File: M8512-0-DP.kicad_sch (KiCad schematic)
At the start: 1 part, among them J1 KL10_6-bay_backplane_connector

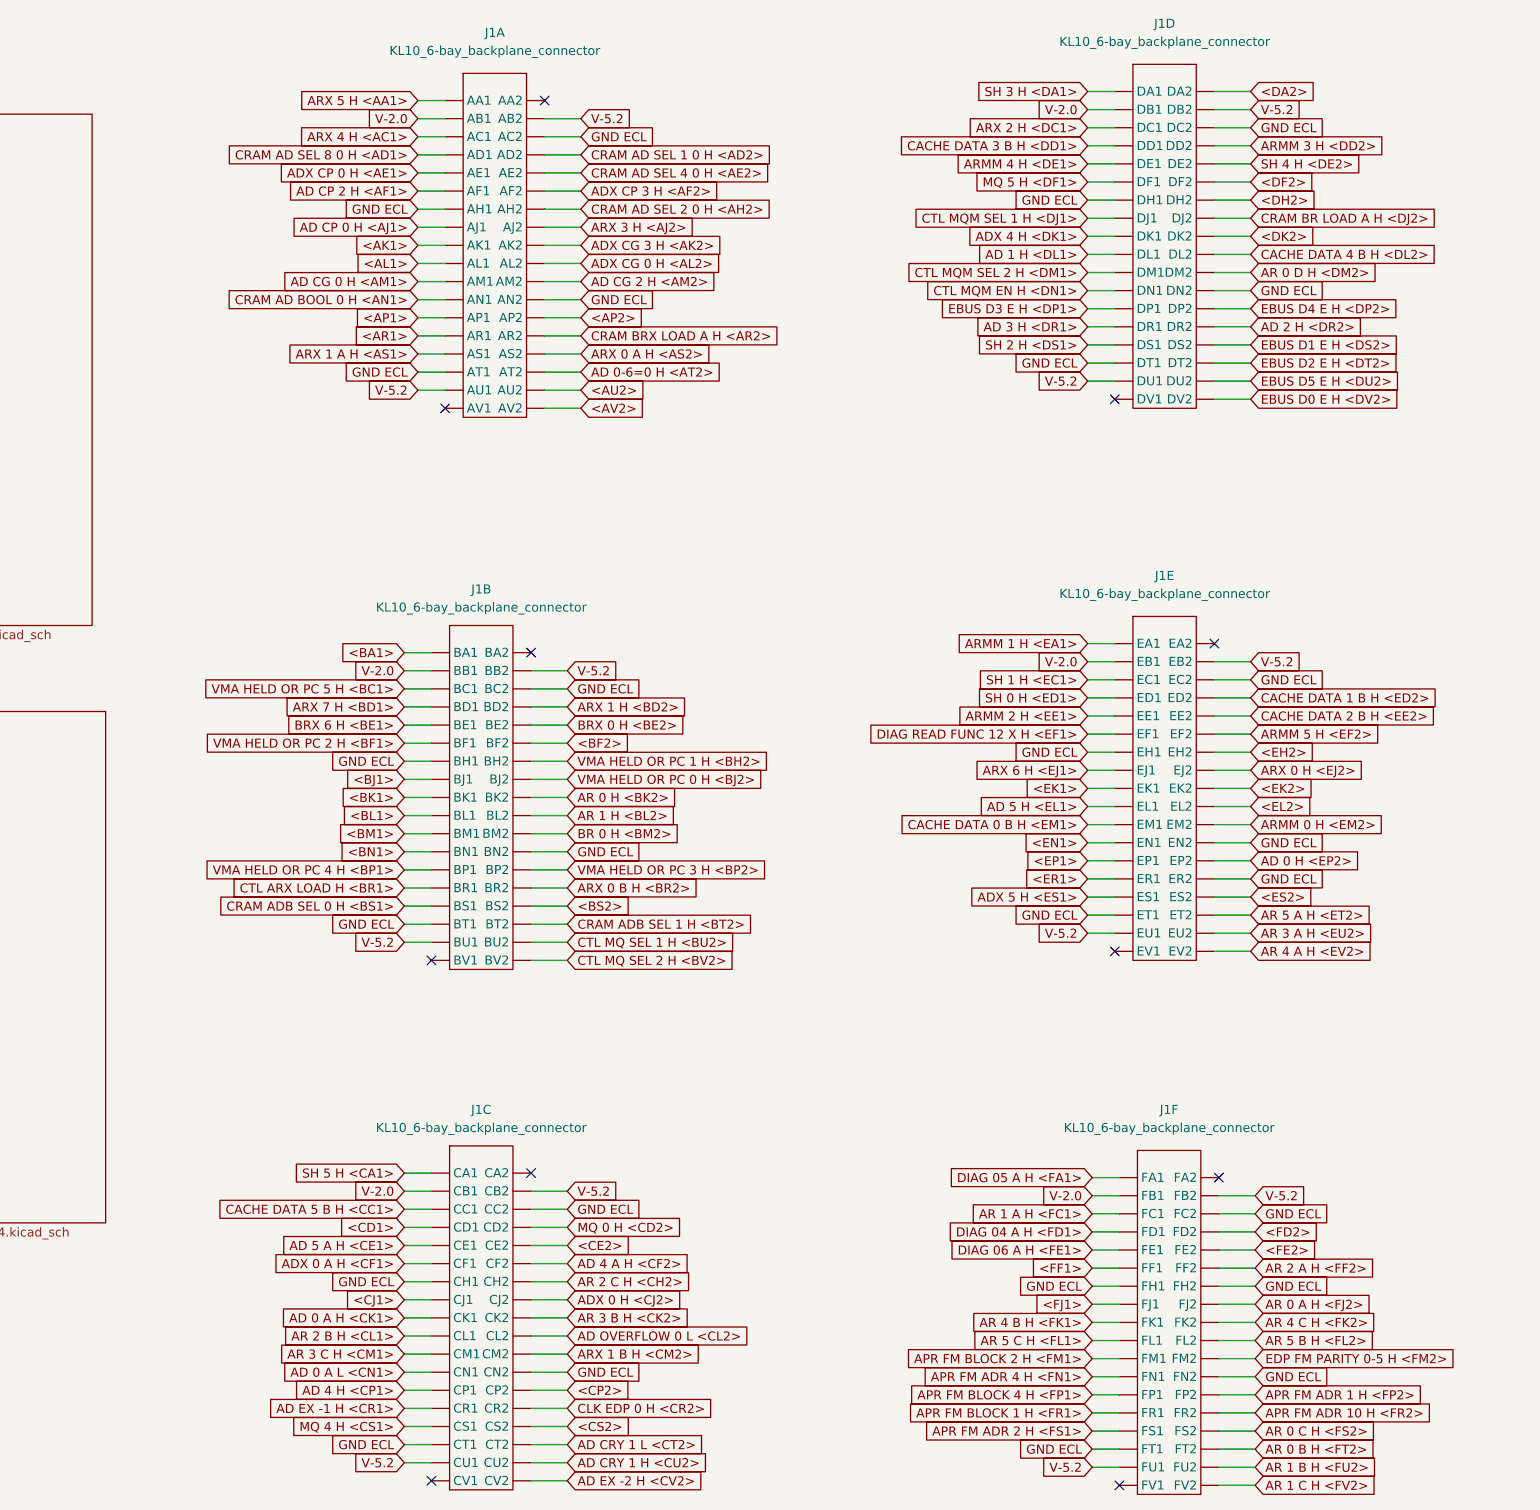
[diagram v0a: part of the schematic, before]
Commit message: Fix a bunch of typos, add ${N} macros for slot specific net names
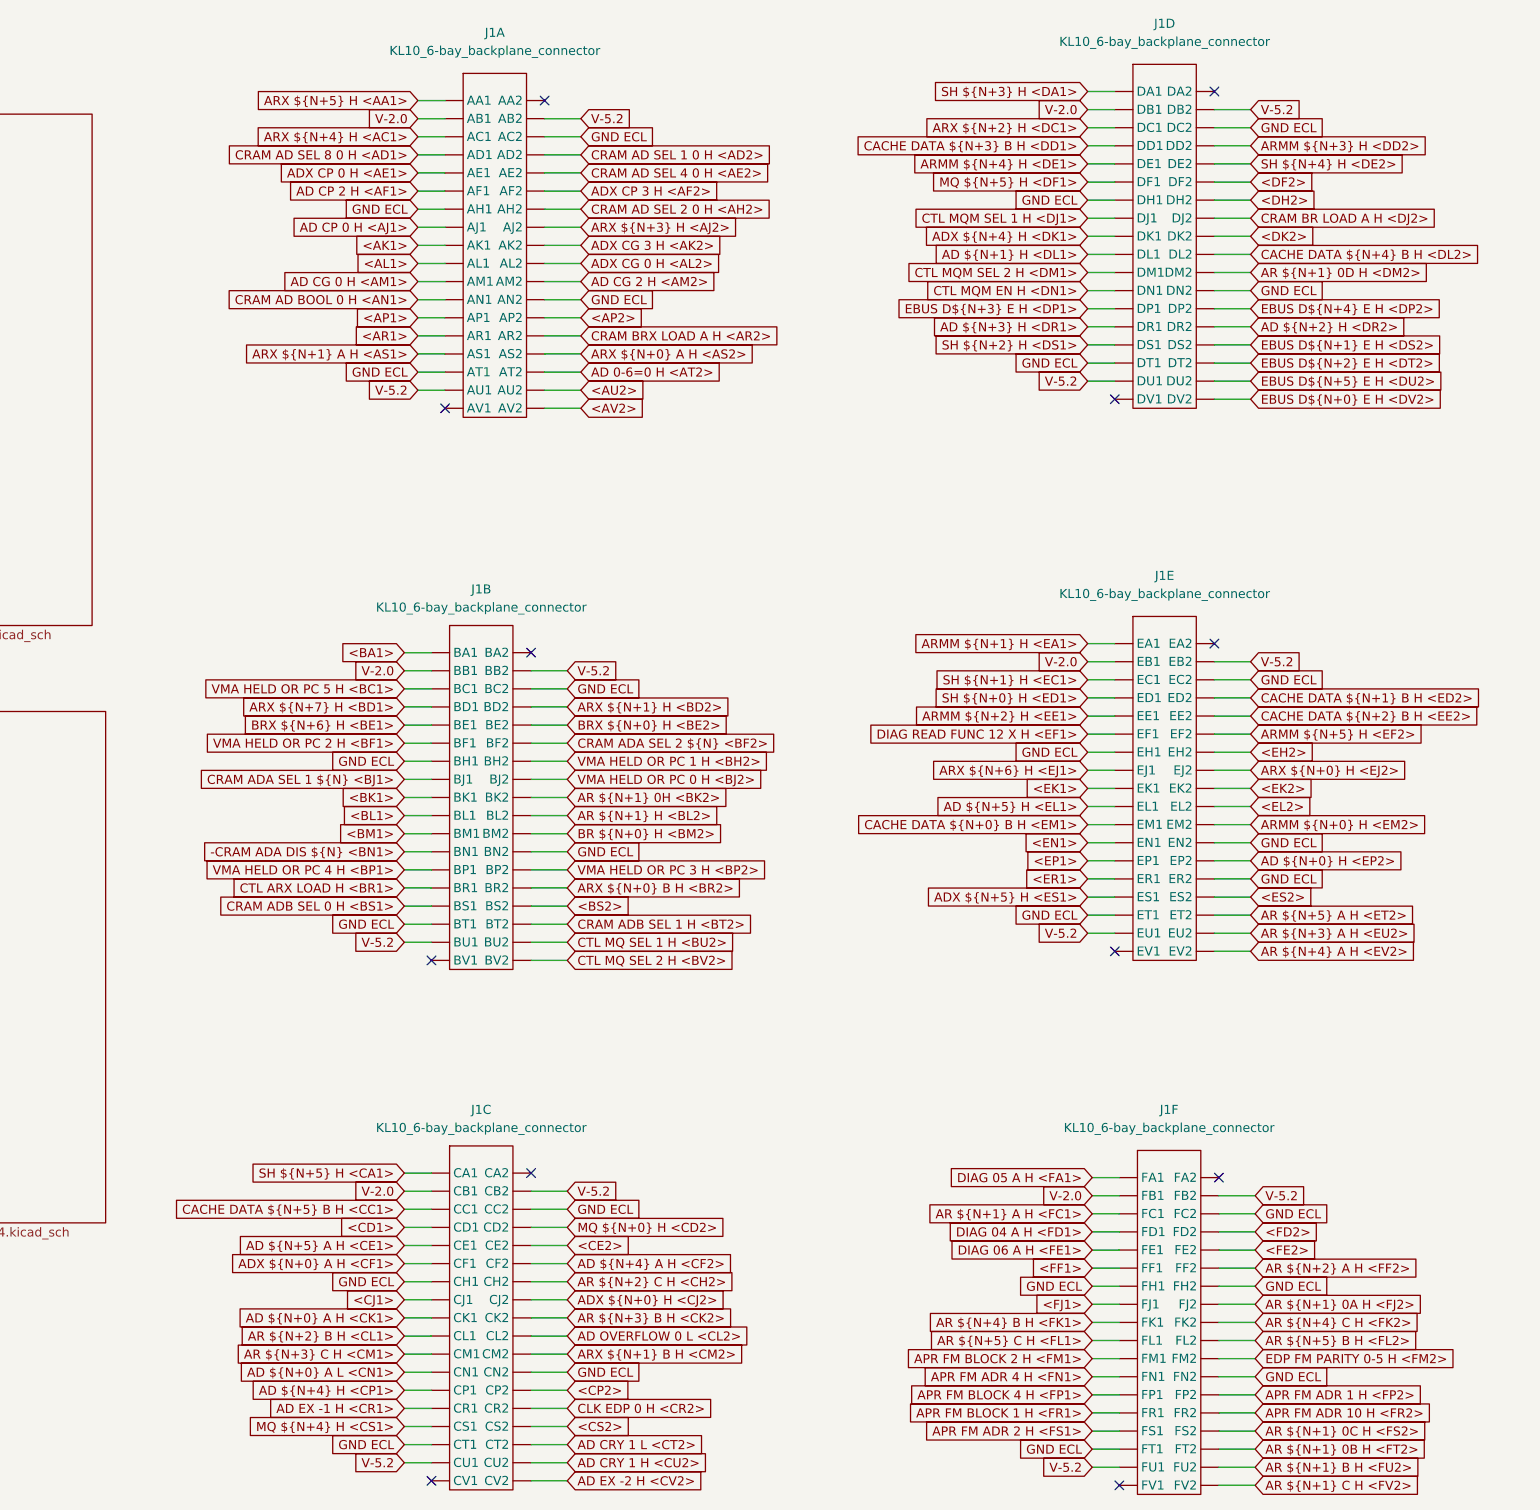
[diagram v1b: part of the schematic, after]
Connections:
- net <BF2> renamed CRAM ADA SEL 2 ${N} <BF2>
- net <BJ1> renamed CRAM ADA SEL 1 ${N} <BJ1>
- net <BN1> renamed -CRAM ADA DIS ${N} <BN1>
- net <DA2>: no longer names the net of J1.110 (DA2)
- net AD 0 A H <CK1> renamed AD ${N+0} A H <CK1>
- net AD 0 A L <CN1> renamed AD ${N+0} A L <CN1>
- net AD 0 H <EP2> renamed AD ${N+0} H <EP2>
- net AD 1 H <DL1> renamed AD ${N+1} H <DL1>
- net AD 2 H <DR2> renamed AD ${N+2} H <DR2>
- net AD 3 H <DR1> renamed AD ${N+3} H <DR1>
- net AD 4 A H <CF2> renamed AD ${N+4} A H <CF2>
- net AD 4 H <CP1> renamed AD ${N+4} H <CP1>
- net AD 5 A H <CE1> renamed AD ${N+5} A H <CE1>
- net AD 5 H <EL1> renamed AD ${N+5} H <EL1>
- net ADX 0 A H <CF1> renamed ADX ${N+0} A H <CF1>
- net ADX 0 H <CJ2> renamed ADX ${N+0} H <CJ2>
- net ADX 4 H <DK1> renamed ADX ${N+4} H <DK1>
- net ADX 5 H <ES1> renamed ADX ${N+5} H <ES1>
- net AR 0 A H <FJ2> renamed AR ${N+1} 0A H <FJ2>
- net AR 0 B H <FT2> renamed AR ${N+1} 0B H <FT2>
- net AR 0 C H <FS2> renamed AR ${N+1} 0C H <FS2>
- net AR 0 D H <DM2> renamed AR ${N+1} 0D H <DM2>
- net AR 0 H <BK2> renamed AR ${N+1} 0H <BK2>
- net AR 1 A H <FC1> renamed AR ${N+1} A H <FC1>
- net AR 1 B H <FU2> renamed AR ${N+1} B H <FU2>
- net AR 1 C H <FV2> renamed AR ${N+1} C H <FV2>
- net AR 1 H <BL2> renamed AR ${N+1} H <BL2>
- net AR 2 A H <FF2> renamed AR ${N+2} A H <FF2>
- net AR 2 B H <CL1> renamed AR ${N+2} B H <CL1>
- net AR 2 C H <CH2> renamed AR ${N+2} C H <CH2>
- net AR 3 A H <EU2> renamed AR ${N+3} A H <EU2>
- net AR 3 B H <CK2> renamed AR ${N+3} B H <CK2>
- net AR 3 C H <CM1> renamed AR ${N+3} C H <CM1>
- net AR 4 A H <EV2> renamed AR ${N+4} A H <EV2>
- net AR 4 B H <FK1> renamed AR ${N+4} B H <FK1>
- net AR 4 C H <FK2> renamed AR ${N+4} C H <FK2>
- net AR 5 A H <ET2> renamed AR ${N+5} A H <ET2>
- net AR 5 B H <FL2> renamed AR ${N+5} B H <FL2>
- net AR 5 C H <FL1> renamed AR ${N+5} C H <FL1>
- net ARMM 0 H <EM2> renamed ARMM ${N+0} H <EM2>
- net ARMM 1 H <EA1> renamed ARMM ${N+1} H <EA1>
- net ARMM 2 H <EE1> renamed ARMM ${N+2} H <EE1>
- net ARMM 3 H <DD2> renamed ARMM ${N+3} H <DD2>
- net ARMM 4 H <DE1> renamed ARMM ${N+4} H <DE1>
- net ARMM 5 H <EF2> renamed ARMM ${N+5} H <EF2>
- net ARX 0 A H <AS2> renamed ARX ${N+0} A H <AS2>
- net ARX 0 B H <BR2> renamed ARX ${N+0} B H <BR2>
- net ARX 0 H <EJ2> renamed ARX ${N+0} H <EJ2>
- net ARX 1 A H <AS1> renamed ARX ${N+1} A H <AS1>
- net ARX 1 B H <CM2> renamed ARX ${N+1} B H <CM2>
- net ARX 1 H <BD2> renamed ARX ${N+1} H <BD2>
- net ARX 2 H <DC1> renamed ARX ${N+2} H <DC1>
- net ARX 3 H <AJ2> renamed ARX ${N+3} H <AJ2>
- net ARX 4 H <AC1> renamed ARX ${N+4} H <AC1>
- net ARX 5 H <AA1> renamed ARX ${N+5} H <AA1>
- net ARX 6 H <EJ1> renamed ARX ${N+6} H <EJ1>
- net ARX 7 H <BD1> renamed ARX ${N+7} H <BD1>
- net BR 0 H <BM2> renamed BR ${N+0} H <BM2>
- net BRX 0 H <BE2> renamed BRX ${N+0} H <BE2>
- net BRX 6 H <BE1> renamed BRX ${N+6} H <BE1>
- net CACHE DATA 0 B H <EM1> renamed CACHE DATA ${N+0} B H <EM1>
- net CACHE DATA 1 B H <ED2> renamed CACHE DATA ${N+1} B H <ED2>
- net CACHE DATA 2 B H <EE2> renamed CACHE DATA ${N+2} B H <EE2>
- net CACHE DATA 3 B H <DD1> renamed CACHE DATA ${N+3} B H <DD1>
- net CACHE DATA 4 B H <DL2> renamed CACHE DATA ${N+4} B H <DL2>
- net CACHE DATA 5 B H <CC1> renamed CACHE DATA ${N+5} B H <CC1>
- net EBUS D0 E H <DV2> renamed EBUS D${N+0} E H <DV2>
- net EBUS D1 E H <DS2> renamed EBUS D${N+1} E H <DS2>
- net EBUS D2 E H <DT2> renamed EBUS D${N+2} E H <DT2>
- net EBUS D3 E H <DP1> renamed EBUS D${N+3} E H <DP1>
- net EBUS D4 E H <DP2> renamed EBUS D${N+4} E H <DP2>
- net EBUS D5 E H <DU2> renamed EBUS D${N+5} E H <DU2>
- net MQ 0 H <CD2> renamed MQ ${N+0} H <CD2>
- net MQ 4 H <CS1> renamed MQ ${N+4} H <CS1>
- net MQ 5 H <DF1> renamed MQ ${N+5} H <DF1>
- net SH 0 H <ED1> renamed SH ${N+0} H <ED1>
- net SH 1 H <EC1> renamed SH ${N+1} H <EC1>
- net SH 2 H <DS1> renamed SH ${N+2} H <DS1>
- net SH 3 H <DA1> renamed SH ${N+3} H <DA1>
- net SH 4 H <DE2> renamed SH ${N+4} H <DE2>
- net SH 5 H <CA1> renamed SH ${N+5} H <CA1>
- no-connect marks 11 -> 12

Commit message: Now DP02 is done, but still need to do DP03/4 and relabel J1 net names to match.
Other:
- note added: "TODO: Change net names for <xxn> labels to match ${...} labels added in sheets."
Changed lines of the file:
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@@
     (stroke (width 0) (type default) (color 0 0 0 0))
+  )
+  (text "TODO: Change net names for <xxn> labels to match ${...} labels added in sheets."
+    (at 78.105 97.79 0)
+    (effects (font (size 5.08 5.08)) (justify left bottom))
   )
   (global_label "V-5.2" (shape input) (at 327.66 33.655 0) (fields_autoplaced)

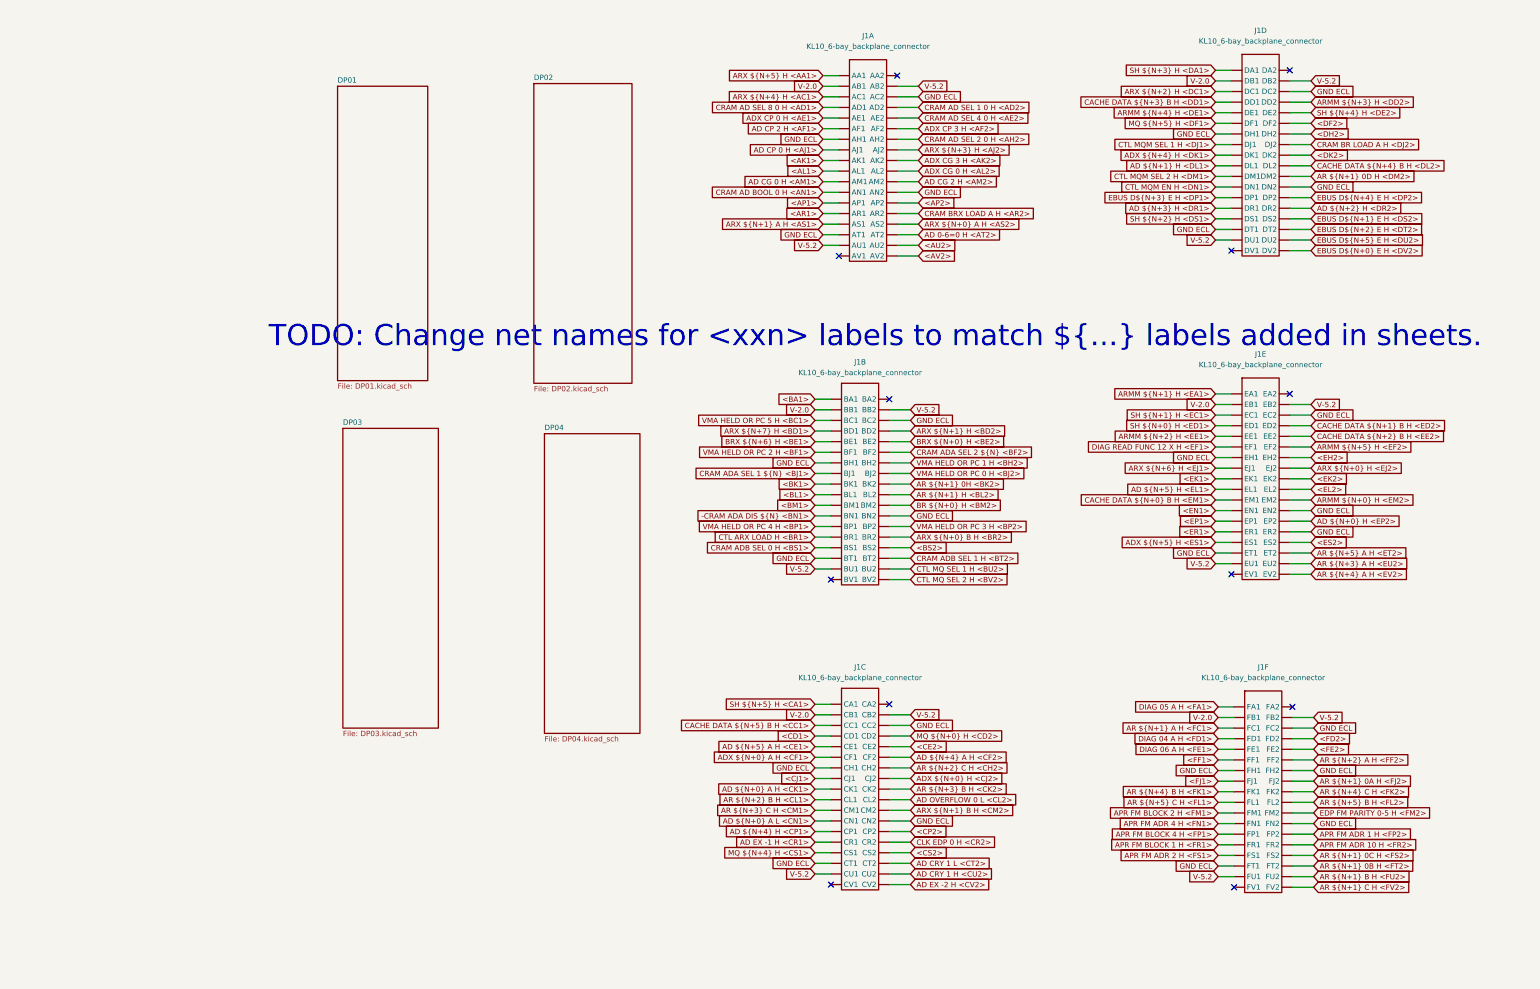
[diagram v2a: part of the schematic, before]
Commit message: I think all pages now have ${N+x} stuff, but still need to relabel J1 net names to match.
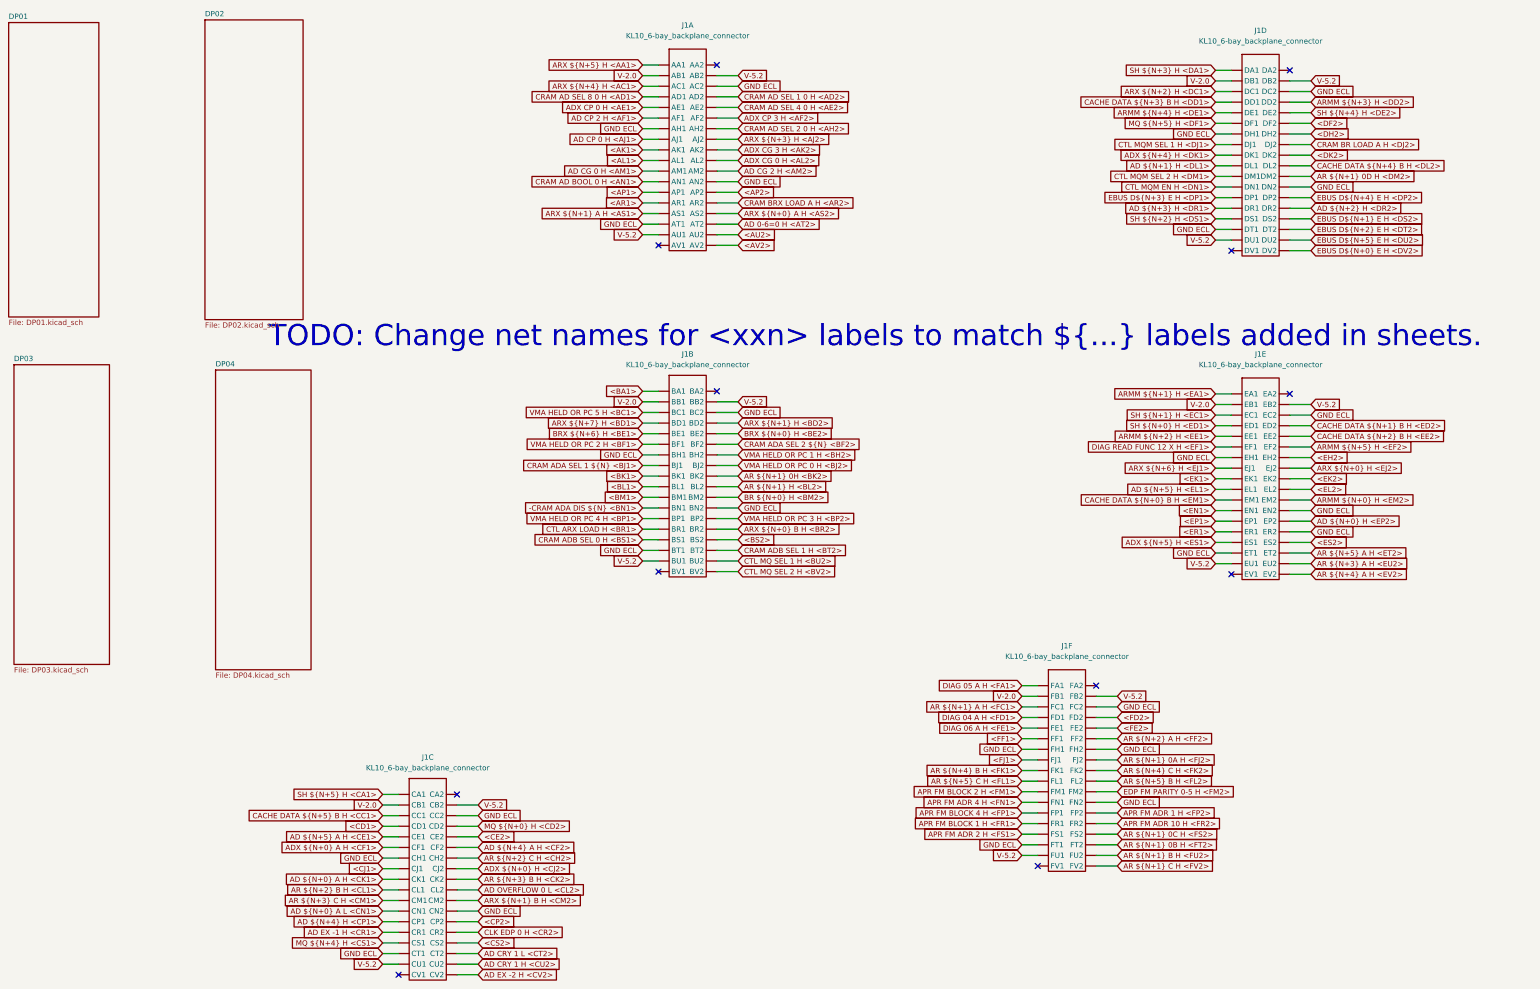
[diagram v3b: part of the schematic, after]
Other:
- moved on the sheet: J1A, J1B, J1C, J1F
